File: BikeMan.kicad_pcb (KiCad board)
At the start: 2 copper layers, 152.4 x 127 mm, 98 parts, among them J1 USB_A_stacked, J10 Conn_01x06_Male, J11 Conn_01x06_Male, J12 MagJack, J13 Micro_SD_Card_Det, J14 HDMI_A_1.4, J2 USB_A_stacked, J3 Barrel_Jack, J4 Conn_01x06_Female, J5 Conn_01x06_Female, J6 Conn_01x06_Female, J7 PushConnector_8pos, J8 PushConnector_8pos, J9 PushConnector_8pos, Q1 AUIRF7316QTR, Q2 AUIRF7316QTR, Q3 AUIRF7316QTR, Q4 AUIRF7316QTR, Q5 DMN62D0U-7, Q6 DMN62D0U-7, U1 RT9742GGJ5, U2 TUSB2046IBVF, U3 AP64501, U4 MCP2515, U5 MCP2551, U6 NPIC6C596ADJ, U7 PCF8574DWR, U8 PCF85063A, Y1 ABLS7M-16.000MHZ-B-2-T

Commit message: Finished trace routing
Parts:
- added C4: C, Capacitor_SMD:C_0805_2012Metric, B.Cu at (156.3, 120.3)
- added C5: C, Capacitor_SMD:C_0805_2012Metric, B.Cu at (173.5, 125.5)
- added C6: C, Capacitor_SMD:C_0805_2012Metric, B.Cu at (170.2, 125.5)
- added C8: C, Capacitor_SMD:C_0805_2012Metric, F.Cu at (173.5, 135.3)
- added JP1: SolderJumper_3_Open, Jumper:SolderJumper-3_P1.3mm_Open_RoundedPad1.0x1.5mm_NumberLabels, F.Cu at (147.4, 127.9)
- added JP6: SolderJumper_3_Open, Jumper:SolderJumper-3_P1.3mm_Open_RoundedPad1.0x1.5mm_NumberLabels, F.Cu at (90.3, 101.2)
- added JP7: SolderJumper_3_Open, Jumper:SolderJumper-3_P1.3mm_Open_RoundedPad1.0x1.5mm_NumberLabels, F.Cu at (86.9, 101.2)
- added R11: R, Resistor_SMD:R_0805_2012Metric, B.Cu at (156.3, 122.3)
- added R12: R, Resistor_SMD:R_0805_2012Metric, F.Cu at (165.4, 135.3)
- added R13: R, Resistor_SMD:R_0805_2012Metric, F.Cu at (167.4, 135.3)
- added R14: R, Resistor_SMD:R_0805_2012Metric, F.Cu at (169.4, 135.3)
- added R17: R, Resistor_SMD:R_0805_2012Metric, F.Cu at (171.4, 135.3)
- added TP5: TestPoint, TestPoint:TestPoint_Pad_D1.5mm, F.Cu at (162.6, 125.6)
- added TP6: TestPoint, TestPoint:TestPoint_Pad_D1.5mm, F.Cu at (176.8, 132.0)
- added TP7: TestPoint, TestPoint:TestPoint_Pad_D1.5mm, F.Cu at (179.5, 132.1)
- added U10: TCN75, Package_SO:SOIC-8_3.9x4.9mm_P1.27mm, F.Cu at (97.3, 100.9)
- added U3: TPS2044BD, Package_SO:SOIC-16_3.9x9.9mm_P1.27mm, B.Cu at (168.4, 133.5)
- added Y1: HC49USM-FF3F18-6.000MHZ, Crystal:Crystal_SMD_HC49-SD, F.Cu at (172.0, 128.5)
- added Y3: Crystal-CM7V-T1A-32.768kHz, footprints:Crystal-CM7V, F.Cu at (196.1, 112.4)
- C10: renamed from C6; value 10uF -> CAP-CERAMIC-10uF
- C11: renamed from C8; value 10nF -> C
- C13: renamed from C9; value 100nF -> C
- C15: renamed from C16; value 10uF -> CAP-CERAMIC-10uF
- C16: renamed from C17; value 10uF -> CAP-CERAMIC-10uF
- C17: renamed from C18; value 10uF -> CAP-CERAMIC-10uF
- C24: renamed from C15; moved to B.Cu
- C7: renamed from C21; value 0.1uF -> C; moved to B.Cu
- R21: renamed from R20; value 10k -> R
- R22: renamed from R21; value 22k -> R
- moved C7 10.1 mm to (155.1, 126.5)
- moved U9 6.09 mm to (196.8, 105.9), turned to 90 degrees
- moved D9 4.60 mm to (191.7, 100.3)
- moved R22 4.05 mm to (89.5, 54.5)
- moved C24 3.82 mm to (195.6, 75.7), turned to 180 degrees
- moved U2 3.44 mm to (156.8, 130.7)
- moved BT1 3.33 mm to (197.3, 90.4)
- renumbered C7 to C12, C10 to C14, C19 to C18, C11 to C19, C12 to C20, C13 to C21, C20 to C22, C14 to C23, C4 to C3, C5 to C9, D8 to D2, D9 to D3, D2 to D4, D3 to D5, D4 to D6, D5 to D7, D6 to D8, D7 to D9, J5 to J4, J4 to J5, JP1 to JP2, JP2 to JP5, Q5 to Q1, Q6 to Q2, Q1 to Q3, Q2 to Q4, Q3 to Q5, Q4 to Q6, R18 to R1, R8 to R10, R9 to R18, R10 to R19, R19 to R2, R11 to R20, R12 to R23, R13 to R24, R14 to R25, R17 to R26, R1 to R3, R2 to R4, R3 to R5, R4 to R6, R5 to R7, R6 to R8, R7 to R9, TP2 to TP10, TP3 to TP11, TP4 to TP12, TP5 to TP13, TP6 to TP14, TP7 to TP15, TP8 to TP16, TP1 to TP9, U3 to U4, U4 to U5, U5 to U6, U6 to U7, U7 to U8, U8 to U9, Y1 to Y2
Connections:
- net /ComputeModule_B/USB_{D+} renamed /ComputeModule_B/USB_D+
- net /ComputeModule_B/USB_{D-} renamed /ComputeModule_B/USB_D-
- net /RealTimeClock/RTC_power renamed /I2C extras/RTC_power
- net Net-(D1-Pad2) renamed /PWR_IN
- H1 pad 1: no_connect_211 -> no_connect_185
- H2 pad 1: no_connect_212 -> no_connect_186
- H3 pad 1: no_connect_213 -> no_connect_187
- H4 pad 1: no_connect_214 -> no_connect_188
- J1 pad 1: /D_{2}+ -> /PWR_{4}
- J1 pad 2: Net-(J1-Pad2) -> /D_{3}-
- J1 pad 3: /D_{2}- -> /D_{3}+
- J1 pad 5: +5V -> /PWR_{3}
- J1 pad 6: /D_{1}- -> /D_{4}-
- J1 pad 7: /D_{1}+ -> /D_{4}+
- J12 pad 1: no_connect_215 -> no_connect_189
- J12 pad 8: no_connect_217 -> no_connect_191
- J2 pad 1: +5V -> /PWR_{2}
- J2 pad 2: /D_{4}- -> /D_{2}-
- J2 pad 3: /D_{4}+ -> /D_{2}+
- J2 pad 5: +5V -> /PWR_{1}
- J2 pad 6: /D_{3}- -> /D_{1}-
- J2 pad 7: /D_{3}+ -> /D_{1}+
- J6 pad 2: /ES.GPIO_{1} -> /ES.GPIO_{2}
- J6 pad 3: /ES.GPIO_{2} -> /ES.GPIO_{3}
- J6 pad 4: /ES.GPIO_{3} -> /ES.GPIO_{1}
- Module1 pad 10: no_connect_218 -> no_connect_192
- Module1 pad 102: no_connect_219 -> no_connect_193
- Module1 pad 104: no_connect_220 -> no_connect_194
- Module1 pad 106: no_connect_221 -> no_connect_195
- Module1 pad 109: no_connect_222 -> no_connect_196
- Module1 pad 110: no_connect_223 -> no_connect_197
- Module1 pad 111: no_connect_224 -> no_connect_198
- Module1 pad 112: no_connect_225 -> no_connect_199
- Module1 pad 115: no_connect_226 -> no_connect_200
- Module1 pad 116: no_connect_227 -> no_connect_201
- Module1 pad 117: no_connect_228 -> no_connect_202
- Module1 pad 118: no_connect_229 -> no_connect_203
- Module1 pad 12: no_connect_230 -> no_connect_204
- Module1 pad 121: no_connect_231 -> no_connect_205
- Module1 pad 122: no_connect_232 -> no_connect_206
- Module1 pad 123: no_connect_233 -> no_connect_207
- Module1 pad 124: no_connect_234 -> no_connect_208
- Module1 pad 127: no_connect_235 -> no_connect_209
- Module1 pad 128: no_connect_236 -> no_connect_210
- Module1 pad 129: no_connect_237 -> no_connect_211
- Module1 pad 130: no_connect_238 -> no_connect_212
- Module1 pad 133: no_connect_239 -> no_connect_213
- Module1 pad 134: no_connect_240 -> no_connect_214
- Module1 pad 135: no_connect_241 -> no_connect_215
- Module1 pad 136: no_connect_242 -> no_connect_216
- Module1 pad 139: no_connect_243 -> no_connect_217
- Module1 pad 14: Net-(Module1-Pad14) -> GND
- Module1 pad 140: no_connect_244 -> no_connect_218
- Module1 pad 141: no_connect_245 -> no_connect_219
- Module1 pad 142: no_connect_246 -> no_connect_220
- Module1 pad 143: no_connect_247 -> no_connect_221
- Module1 pad 145: no_connect_248 -> no_connect_222
- Module1 pad 146: no_connect_249 -> no_connect_223
- Module1 pad 147: no_connect_250 -> no_connect_224
- Module1 pad 148: no_connect_251 -> no_connect_225
- Module1 pad 149: no_connect_252 -> no_connect_226
- Module1 pad 152: no_connect_253 -> no_connect_227
- Module1 pad 154: no_connect_254 -> no_connect_228
- Module1 pad 157: no_connect_255 -> no_connect_229
- Module1 pad 158: no_connect_256 -> no_connect_230
- Module1 pad 159: no_connect_257 -> no_connect_231
- Module1 pad 160: no_connect_258 -> no_connect_232
- Module1 pad 163: no_connect_259 -> no_connect_233
- Module1 pad 164: no_connect_260 -> no_connect_234
- Module1 pad 165: no_connect_261 -> no_connect_235
- Module1 pad 166: no_connect_262 -> no_connect_236
- Module1 pad 169: no_connect_263 -> no_connect_237
- Module1 pad 171: no_connect_264 -> no_connect_238
- Module1 pad 175: no_connect_265 -> no_connect_239
- Module1 pad 177: no_connect_266 -> no_connect_240
- Module1 pad 181: no_connect_267 -> no_connect_241
- Module1 pad 183: no_connect_268 -> no_connect_242
- Module1 pad 187: no_connect_269 -> no_connect_243
- Module1 pad 189: no_connect_270 -> no_connect_244
- Module1 pad 19: no_connect_271 -> no_connect_245
- Module1 pad 193: no_connect_272 -> no_connect_246
- Module1 pad 195: no_connect_273 -> no_connect_247
- Module1 pad 2: Net-(Module1-Pad2) -> GND
- Module1 pad 22: Net-(Module1-Pad22) -> GND
- Module1 pad 28: Net-(Module1-Pad28) -> /GPIO_{sCLK}
- Module1 pad 29: Net-(Module1-Pad29) -> /ES.GPIO_{4}
- Module1 pad 3: no_connect_274 -> no_connect_248
- Module1 pad 30: Net-(Module1-Pad30) -> /GPIO_{rCLK}
- Module1 pad 31: Net-(Module1-Pad31) -> /ES.GPIO_{5}
- Module1 pad 32: Net-(Module1-Pad32) -> GND
- Module1 pad 34: Net-(Module1-Pad34) -> /~GPIO_{OE}
- Module1 pad 35: Net-(Module1-Pad35) -> no_connect_249
- Module1 pad 36: Net-(Module1-Pad36) -> no_connect_250
- Module1 pad 37: Net-(Module1-Pad37) -> /ES.GPIO_{1}
- Module1 pad 38: Net-(Module1-Pad38) -> /~GPIO_{RS}
- Module1 pad 39: Net-(Module1-Pad39) -> /ES.GPIO_{2}
- Module1 pad 40: Net-(Module1-Pad40) -> /GPIO_{DATA}
- Module1 pad 41: Net-(Module1-Pad41) -> /ES.GPIO_{3}
- Module1 pad 42: Net-(Module1-Pad42) -> GND
- Module1 pad 5: no_connect_275 -> no_connect_251
- Module1 pad 52: Net-(Module1-Pad52) -> GND
- Module1 pad 56: Net-(Module1-Pad56) -> /SCL_{3.3V}
- Module1 pad 58: Net-(Module1-Pad58) -> /SDA_{3.3V}
- Module1 pad 60: Net-(Module1-Pad60) -> GND
- Module1 pad 66: Net-(Module1-Pad66) -> GND
- Module1 pad 74: Net-(Module1-Pad74) -> GND
- Module1 pad 8: Net-(Module1-Pad8) -> GND
- Module1 pad 80: /SCL_{3.3V} -> Net-(Module1-Pad80)
- Module1 pad 82: /SDA_{3.3V} -> Net-(Module1-Pad82)
- Module1 pad 98: Net-(Module1-Pad98) -> GND
- U2 pad 10: Net-(U2-Pad10) -> /ComputeModule_B/~OC1
- U2 pad 11: /D_{1}+ -> /D_{2}-
- U2 pad 12: /D_{1}+ -> /D_{2}+
- U2 pad 14: Net-(U2-Pad14) -> /ComputeModule_B/~OC2
- U2 pad 15: /D_{2}+ -> /D_{1}-
- U2 pad 16: /D_{2}+ -> /D_{1}+
- U2 pad 18: Net-(U2-Pad18) -> /ComputeModule_B/~OC3
- U2 pad 19: /D_{3}+ -> /D_{3}-
- U2 pad 22: Net-(U2-Pad22) -> /ComputeModule_B/~OC4
- U2 pad 23: /D_{4}+ -> /D_{4}-
- U2 pad 25: Net-(U2-Pad25) -> +3V3
- U2 pad 27: Net-(U2-Pad27) -> GND
- U2 pad 28: Net-(U2-Pad28) -> GND
- U2 pad 29: Net-(U2-Pad29) -> /ComputeModule_B/XTAL2
- U2 pad 3: Net-(U2-Pad3) -> +3V3
- U2 pad 30: Net-(U2-Pad30) -> /ComputeModule_B/XTAL1
- U2 pad 31: Net-(U2-Pad31) -> GND
- U2 pad 32: Net-(U2-Pad32) -> /ComputeModule_B/SUSPND
- U2 pad 4: Net-(U2-Pad4) -> /ComputeModule_B/~Reset
- U2 pad 5: no_connect_276 -> no_connect_253
- U2 pad 7: Net-(U2-Pad7) -> GND
- U5 pad 10: no_connect_277 -> no_connect_254
- U5 pad 11: no_connect_278 -> no_connect_255
- U5 pad 3: no_connect_279 -> no_connect_256
- U5 pad 4: no_connect_280 -> no_connect_257
- U5 pad 5: no_connect_281 -> no_connect_258
- U5 pad 6: no_connect_282 -> no_connect_259
- U6 pad 5: no_connect_283 -> no_connect_260
- U7 pad 9: no_connect_284 -> no_connect_261
- U9 pad 1: /RealTimeClock/osc_in -> /I2C extras/osc_in
- U9 pad 2: /RealTimeClock/osc_out -> /I2C extras/osc_out
- U9 pad 3: no_connect_285 -> no_connect_262
- U9 pad 5: /SDA -> /SDA_{3.3V}
- U9 pad 6: /SCL -> /SCL_{3.3V}
- U9 pad 7: no_connect_286 -> no_connect_263
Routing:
- net +3V3: track 26.4 -> 336.4 mm, vias 2 -> 13
- net GND: track 28.1 -> 216.2 mm, vias 11 -> 43
- net +5V: track 17.8 -> 133.7 mm, vias 2 -> 20
- net /SDA_{3.3V}: track 1.72 -> 96.1 mm, vias 0 -> 4
- net /SCL_{3.3V}: track 2.39 -> 93.4 mm, vias 0 -> 4
- net /~GPIO_{OE}: track 0.00 -> 72.9 mm, vias 0 -> 2
- net /~GPIO_{RS}: track 0.00 -> 72.6 mm, vias 0 -> 2
- net /GPIO_{rCLK}: track 0.00 -> 68.3 mm, vias 0 -> 2
- net /GPIO_{DATA}: track 0.00 -> 65.8 mm, vias 0 -> 2
- net /GPIO_{sCLK}: track 0.00 -> 61.1 mm, vias 0 -> 2
- net /ComputeModule_B/USB_D-: track 0.00 -> 44.1 mm
- net /ComputeModule_B/USB_D+: track 0.00 -> 43.3 mm
- net /PWR_{1}: track 0.00 -> 38.0 mm
- net Net-(BT1-Pad1): track 0.00 -> 30.8 mm
- net Net-(U2-Pad21): track 0.00 -> 28.6 mm, vias 0 -> 1
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- added copper zone on F.Cu, net +3V3
- added copper zone on B.Cu, net +5V
- added copper zone on F.Cu, net /PWR_IN
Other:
- board text added: "Address Select"

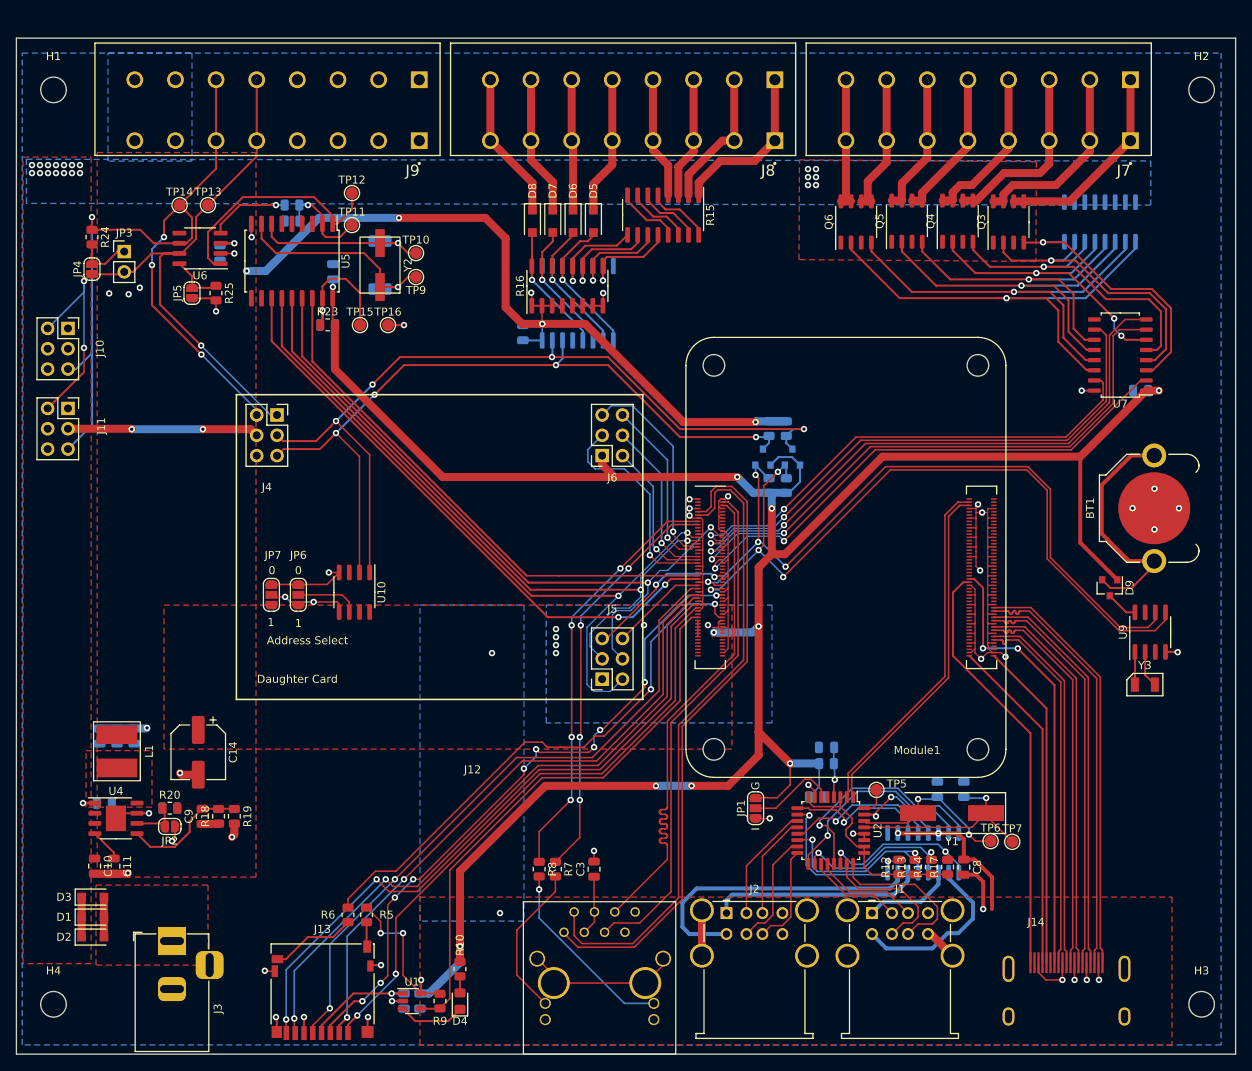
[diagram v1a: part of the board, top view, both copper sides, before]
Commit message: Cleaning up
Reassigned reference designators to better match their position on the board.
Moved USB hub IC and related circuits to their own sheet in the schematic.
Tweaked reference designator positions on board to improve visibility.
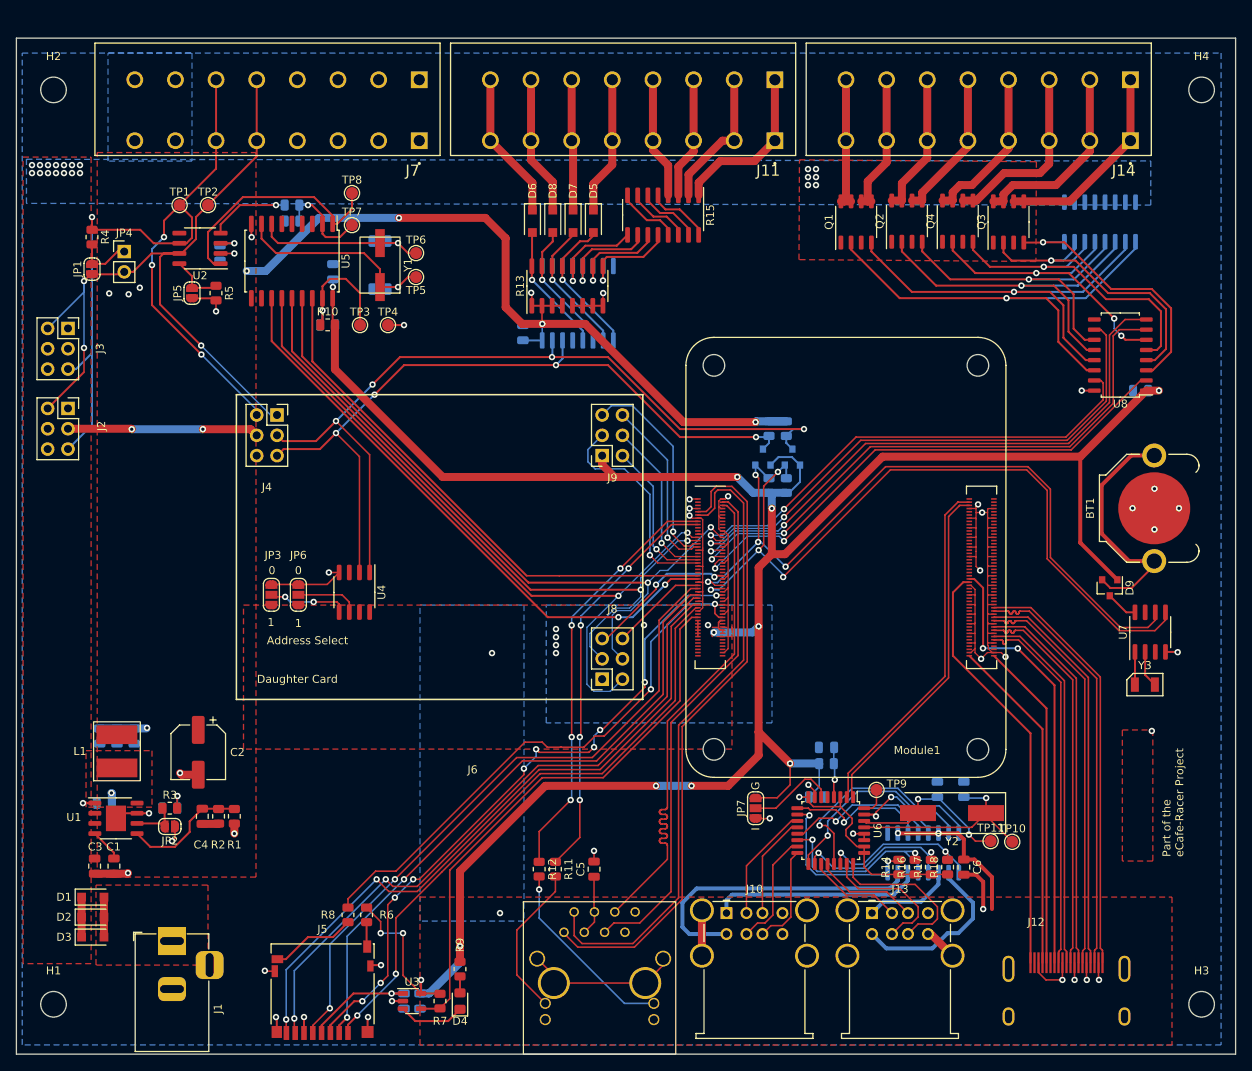
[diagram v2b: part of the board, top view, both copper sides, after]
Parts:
- C19: renamed from C16; value CAP-CERAMIC-10uF -> 10uF
- C21: renamed from C17; value CAP-CERAMIC-10uF -> 10uF
- C22: renamed from C15; value CAP-CERAMIC-10uF -> 10uF
- C3: renamed from C10; value CAP-CERAMIC-10uF -> 10uF
- renumbered C11 to C1, C4 to C10, C7 to C11, C23 to C12, C2 to C13, C1 to C14, C21 to C15, C19 to C16, C20 to C17, C14 to C2, C12 to C20, C13 to C23, C22 to C24, C9 to C4, C3 to C5, C8 to C6, C24 to C7, C5 to C8, C6 to C9, D3 to D1, D1 to D2, D2 to D3, D8 to D6, D6 to D7, D7 to D8, H4 to H1, H1 to H2, H2 to H4, J3 to J1, J2 to J10, J8 to J11, J14 to J12, J1 to J13, J7 to J14, J11 to J2, J10 to J3, J13 to J5, J12 to J6, J9 to J7, J5 to J8, J6 to J9, JP4 to JP1, JP7 to JP3, JP3 to JP4, JP1 to JP7, Q6 to Q1, Q5 to Q2, Q1 to Q5, Q2 to Q6, R19 to R1, R23 to R10, R7 to R11, R8 to R12, R16 to R13, R12 to R14, R13 to R16, R14 to R17, R17 to R18, R26 to R19, R18 to R2, R11 to R20, R1 to R21, R3 to R22, R2 to R23, R4 to R24, R22 to R25, R21 to R26, R20 to R3, R24 to R4, R25 to R5, R5 to R6, R9 to R7, R6 to R8, R10 to R9, TP14 to TP1, TP7 to TP10, TP6 to TP11, TP13 to TP2, TP15 to TP3, TP16 to TP4, TP9 to TP5, TP10 to TP6, TP11 to TP7, TP12 to TP8, TP5 to TP9, U4 to U1, U8 to U10, U6 to U2, U1 to U3, U10 to U4, U2 to U6, U9 to U7, U7 to U8, U3 to U9, Y2 to Y1, Y1 to Y2
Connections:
- net /ComputeModule_B/SUSPND renamed /USB MUX/SUSPND
- net /ComputeModule_B/USB_D+ renamed /USB_D+
- net /ComputeModule_B/USB_D- renamed /USB_D-
- net /ComputeModule_B/XTAL1 renamed /USB MUX/XTAL1
- net /ComputeModule_B/XTAL2 renamed /USB MUX/XTAL2
- net /ComputeModule_B/~OC1 renamed /USB MUX/~OC1
- net /ComputeModule_B/~OC2 renamed /USB MUX/~OC2
- net /ComputeModule_B/~OC3 renamed /USB MUX/~OC3
- net /ComputeModule_B/~OC4 renamed /USB MUX/~OC4
- net /ComputeModule_B/~Reset renamed /USB MUX/~Reset
- net /PWR_IN renamed /Power Supply/PWR_IN
- net /Power/SW renamed /Power Supply/SW
- net /Power/comp renamed /Power Supply/comp
- net /Power/feedback renamed /Power Supply/feedback
- net no_connect_185 renamed no_connect_190
- H1 pad 1: no_connect_188 -> no_connect_189
- H3 pad 1: no_connect_187 -> no_connect_191
- H4 pad 1: no_connect_186 -> no_connect_192
- J6 pad 1: no_connect_189 -> no_connect_193
- J6 pad 8: no_connect_191 -> no_connect_195
- Module1 pad 10: no_connect_192 -> no_connect_196
- Module1 pad 102: no_connect_193 -> no_connect_197
- Module1 pad 104: no_connect_194 -> no_connect_198
- Module1 pad 106: no_connect_195 -> no_connect_199
- Module1 pad 109: no_connect_196 -> no_connect_200
- Module1 pad 110: no_connect_197 -> no_connect_201
- Module1 pad 111: no_connect_198 -> no_connect_202
- Module1 pad 112: no_connect_199 -> no_connect_203
- Module1 pad 115: no_connect_200 -> no_connect_204
- Module1 pad 116: no_connect_201 -> no_connect_205
- Module1 pad 117: no_connect_202 -> no_connect_206
- Module1 pad 118: no_connect_203 -> no_connect_207
- Module1 pad 12: no_connect_204 -> no_connect_208
- Module1 pad 121: no_connect_205 -> no_connect_209
- Module1 pad 122: no_connect_206 -> no_connect_210
- Module1 pad 123: no_connect_207 -> no_connect_211
- Module1 pad 124: no_connect_208 -> no_connect_212
- Module1 pad 127: no_connect_209 -> no_connect_213
- Module1 pad 128: no_connect_210 -> no_connect_214
- Module1 pad 129: no_connect_211 -> no_connect_215
- Module1 pad 130: no_connect_212 -> no_connect_216
- Module1 pad 133: no_connect_213 -> no_connect_217
- Module1 pad 134: no_connect_214 -> no_connect_218
- Module1 pad 135: no_connect_215 -> no_connect_219
- Module1 pad 136: no_connect_216 -> no_connect_220
- Module1 pad 139: no_connect_217 -> no_connect_221
- Module1 pad 140: no_connect_218 -> no_connect_222
- Module1 pad 141: no_connect_219 -> no_connect_223
- Module1 pad 142: no_connect_220 -> no_connect_224
- Module1 pad 143: no_connect_221 -> no_connect_225
- Module1 pad 145: no_connect_222 -> no_connect_226
- Module1 pad 146: no_connect_223 -> no_connect_227
- Module1 pad 147: no_connect_224 -> no_connect_228
- Module1 pad 148: no_connect_225 -> no_connect_229
- Module1 pad 149: no_connect_226 -> no_connect_230
- Module1 pad 152: no_connect_227 -> no_connect_231
- Module1 pad 154: no_connect_228 -> no_connect_232
- Module1 pad 157: no_connect_229 -> no_connect_233
- Module1 pad 158: no_connect_230 -> no_connect_234
- Module1 pad 159: no_connect_231 -> no_connect_235
- Module1 pad 160: no_connect_232 -> no_connect_236
- Module1 pad 163: no_connect_233 -> no_connect_237
- Module1 pad 164: no_connect_234 -> no_connect_238
- Module1 pad 165: no_connect_235 -> no_connect_239
- Module1 pad 166: no_connect_236 -> no_connect_240
- Module1 pad 169: no_connect_237 -> no_connect_241
- Module1 pad 171: no_connect_238 -> no_connect_242
- Module1 pad 175: no_connect_239 -> no_connect_243
- Module1 pad 177: no_connect_240 -> no_connect_244
- Module1 pad 181: no_connect_241 -> no_connect_245
- Module1 pad 183: no_connect_242 -> no_connect_246
- Module1 pad 187: no_connect_243 -> no_connect_247
- Module1 pad 189: no_connect_244 -> no_connect_248
- Module1 pad 19: no_connect_245 -> no_connect_249
- Module1 pad 193: no_connect_246 -> no_connect_250
- Module1 pad 195: no_connect_247 -> no_connect_251
- Module1 pad 3: no_connect_248 -> no_connect_252
- Module1 pad 35: no_connect_249 -> no_connect_253
- Module1 pad 36: no_connect_250 -> no_connect_254
- Module1 pad 5: no_connect_251 -> no_connect_255
- U2 pad 5: no_connect_260 -> no_connect_256
- U4 pad 3: no_connect_252 -> no_connect_257
- U5 pad 10: no_connect_254 -> no_connect_258
- U5 pad 11: no_connect_255 -> no_connect_259
- U5 pad 3: no_connect_256 -> no_connect_260
- U5 pad 4: no_connect_257 -> no_connect_261
- U5 pad 5: no_connect_258 -> no_connect_262
- U5 pad 6: no_connect_259 -> no_connect_263
- U6 pad 23: /D_{4}- -> /D_{4}-_1
- U6 pad 24: /D_{4}+ -> /D_{4}+_1
- U6 pad 5: no_connect_253 -> no_connect_264
- U7 pad 3: no_connect_262 -> no_connect_265
- U7 pad 7: no_connect_263 -> no_connect_266
- U8 pad 9: no_connect_261 -> no_connect_267
- U9 pad 11: /PWR_{4} -> /PWR_{4}_1
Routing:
- net no_connect_193: track 0.00 -> 19.3 mm
- net no_connect_189: track 19.3 -> 0.00 mm
- net Net-(C20-Pad1): track 0.00 -> 3.07 mm, vias 0 -> 1
- net +3V3: track 336.4 -> 338.8 mm, vias 13 -> 14
- net /Power Supply/SW: track 0.00 -> 1.30 mm, vias 0 -> 1
- net GND: track 216.2 -> 215.6 mm, vias 43 -> 44
- added copper zone on F.Cu, net GND
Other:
- board text added: "Dennis v0.1.3"
- board text added: "Part of the eCafe-Racer Project"

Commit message: started cleaning layout
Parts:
- removed C10, C11, C13, C14, C5, C6, C8, C9: C, Capacitor_SMD:C_0805_2012Metric
- removed D4: LED_Red, LED_SMD:LED_0805_2012Metric_Pad1.15x1.40mm_HandSolder
- removed J10, J13: USB_A_stacked, Connector_USB:USB_A_Wuerth_61400826021_Horizontal_Stacked
- removed J12: HDMI_A_1.4, footprints:HDMI_Molex-2086588131
- removed J2, J3: Conn_01x06_Male, Connector_PinSocket_2.54mm:PinSocket_2x03_P2.54mm_Vertical
- removed J4, J9: Conn_01x06_Female, Connector_PinSocket_2.54mm:PinSocket_2x03_P2.54mm_Vertical
- removed J5: Micro_SD_Card_Det, Connector_Card:microSD_HC_Hirose_DM3D-SF
- removed J6: MagJack, footprints:Molex-0936358314
- removed J7: PushConnector_8pos, footprints:CUI_TBL004-508-08BE-2BE
- removed JP7: SolderJumper_3_Open, Jumper:SolderJumper-3_P1.3mm_Open_RoundedPad1.0x1.5mm_NumberLabels
- removed Module1: ComputeModule4-CM4, footprints:Raspberry-Pi-4-Compute-Module
- removed R11, R12, R14, R16, R17, R18, R20, R6, R7, R8, R9: R, Resistor_SMD:R_0805_2012Metric
- removed TP10, TP11, TP9: TestPoint, TestPoint:TestPoint_Pad_D1.5mm
- removed U3: RT9742GGJ5, Package_TO_SOT_SMD:SOT-23-5
- removed U6: TUSB2046IBVF, Package_QFP:LQFP-32_7x7mm_P0.8mm
- removed U9: TPS2044BD, Package_SO:SOIC-16_3.9x9.9mm_P1.27mm
- removed Y2: HC49USM-FF3F18-6.000MHZ, Crystal:Crystal_SMD_HC49-SD
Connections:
- net /CAN Peripherals/~reset renamed /CAN Peripherals/~{reset}
- net /Input_{1} renamed /GPIO/Input_{1}
- net /Input_{2} renamed /GPIO/Input_{2}
- net /Input_{3} renamed /GPIO/Input_{3}
- net /Input_{4} renamed /GPIO/Input_{4}
- net /Input_{5} renamed /GPIO/Input_{5}
- net /Input_{6} renamed /GPIO/Input_{6}
- net /Input_{7} renamed /GPIO/Input_{7}
- net /Input_{8} renamed /GPIO/Input_{8}
- net /OUT_{1} renamed /GPIO/OUT_{1}
- net /OUT_{2} renamed /GPIO/OUT_{2}
- net /OUT_{3} renamed /GPIO/OUT_{3}
- net /OUT_{4} renamed /GPIO/OUT_{4}
- net /OUT_{5} renamed /GPIO/OUT_{5}
- net /OUT_{6} renamed /GPIO/OUT_{6}
- net /OUT_{7} renamed /GPIO/OUT_{7}
- net /OUT_{8} renamed /GPIO/OUT_{8}
- net /~INT_{GPIO} renamed /~{INT_{GPIO}}
- H1 pad 1: no_connect_189 -> unconnected-(H1-Pad1)
- H2 pad 1: no_connect_190 -> unconnected-(H2-Pad1)
- H3 pad 1: no_connect_191 -> unconnected-(H3-Pad1)
- H4 pad 1: no_connect_192 -> unconnected-(H4-Pad1)
- J8 pad 5: /SPI.~CS_{ES1} -> /SPI.~{CS_{ES1}}
- J8 pad 6: /~INT_{ES1} -> /~{INT_{ES1}}
- R26 pad 1: /CAN Peripherals/CAN_{Rx} -> /CAN Peripherals/CAN_{RxLOW}
- R26 pad 2: /CAN Peripherals/CAN_{RxLOW} -> Net-(U2-Pad4)
- U2 pad 1: /CAN Peripherals/CAN_{Tx} -> Net-(U2-Pad1)
- U2 pad 4: /CAN Peripherals/CAN_{Rx} -> Net-(U2-Pad4)
- U2 pad 5: no_connect_256 -> unconnected-(U2-Pad5)
- U4 pad 3: no_connect_257 -> unconnected-(U4-Pad3)
- U5 pad 1: /CAN Peripherals/CAN_{Tx} -> /CAN Peripherals/CAN_{Tx}SPI
- U5 pad 10: no_connect_258 -> unconnected-(U5-Pad10)
- U5 pad 11: no_connect_259 -> unconnected-(U5-Pad11)
- U5 pad 12: /~INT_{CAN} -> /~{INT_{CAN}}
- U5 pad 16: /SPI.~CS_{CAN} -> /SPI.~{CS_{CAN}}
- U5 pad 2: /CAN Peripherals/CAN_{RxLOW} -> /CAN Peripherals/CAN_{Rx}SPI
- U5 pad 3: no_connect_260 -> unconnected-(U5-Pad3)
- U5 pad 4: no_connect_261 -> unconnected-(U5-Pad4)
- U5 pad 5: no_connect_262 -> unconnected-(U5-Pad5)
- U5 pad 6: no_connect_263 -> unconnected-(U5-Pad6)
- U7 pad 3: no_connect_265 -> unconnected-(U7-Pad3)
- U7 pad 7: no_connect_266 -> unconnected-(U7-Pad7)
- U8 pad 7: /~GPIO_{RS} -> /~{GPIO_{RS}}
- U8 pad 8: /~GPIO_{OE} -> /~{GPIO_{OE}}
- U8 pad 9: no_connect_267 -> unconnected-(U8-Pad9)
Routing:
- net +3V3: track 338.8 -> 55.8 mm, vias 14 -> 2
- net GND: track 215.6 -> 56.0 mm, vias 44 -> 20
- net /ComputeModule_A/SD.DAT1: track 84.8 -> 0.00 mm, vias 2 -> 0
- net /ComputeModule_A/SD.DAT0: track 83.6 -> 0.00 mm, vias 2 -> 0
- net /ComputeModule_A/SD.CMD: track 83.1 -> 0.00 mm, vias 10 -> 0
- net /ComputeModule_A/SD.CLK: track 81.6 -> 0.00 mm, vias 2 -> 0
- net /ComputeModule_A/Eth_Rx+: track 80.6 -> 0.00 mm
- net /ComputeModule_A/Eth_Rx-: track 80.3 -> 0.00 mm
- net /ComputeModule_A/SD.DAT3: track 79.3 -> 0.00 mm, vias 2 -> 0
- net /SDA_{3.3V}: track 96.1 -> 19.5 mm, vias 4 -> 0
- net /ComputeModule_A/SD.DAT2: track 76.0 -> 0.00 mm, vias 2 -> 0
- net /SCL_{3.3V}: track 93.4 -> 18.2 mm, vias 4 -> 0
- net /~INT_{CAN}: track 74.9 -> 0.00 mm, vias 2 -> 0
- net /~GPIO_{OE}: track 72.9 -> 0.00 mm, vias 2 -> 0
- net /~GPIO_{RS}: track 72.6 -> 0.00 mm, vias 2 -> 0
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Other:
- board text removed: "Address Select"
- board text removed: "Daughter Card"
